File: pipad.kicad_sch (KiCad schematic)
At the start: 2 parts, among them J3 Conn_02x20_Odd_Even, J5 Conn_01x03

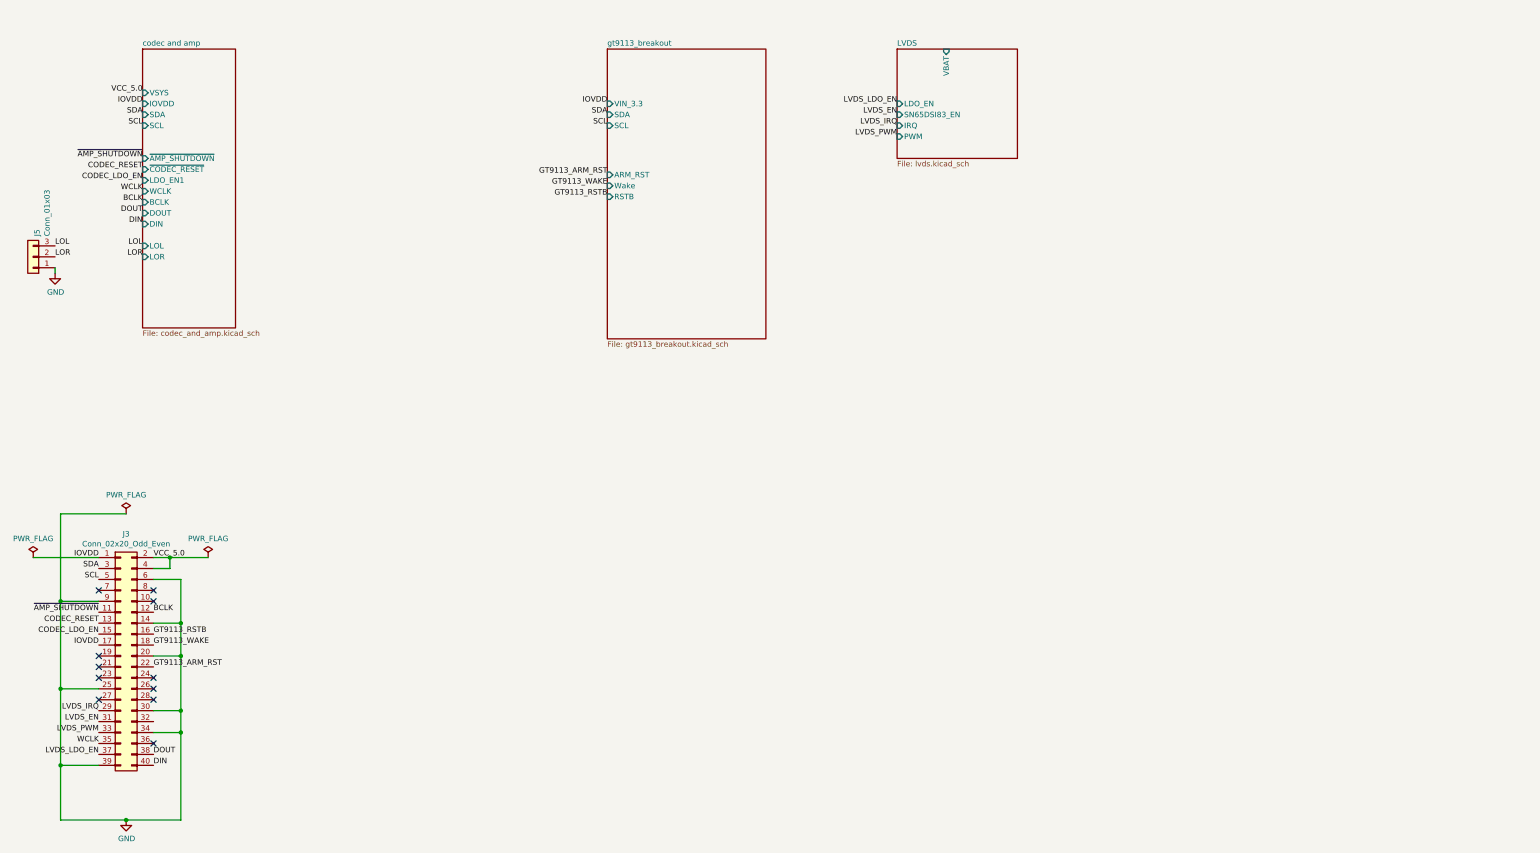
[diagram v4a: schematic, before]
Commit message: Add dock connector, battery pads, and ambient light sensor/compass connector. Switch Pi GPIO header from from THT to SMT so it is easier to place/route. Route differential signals for LVDS converter.
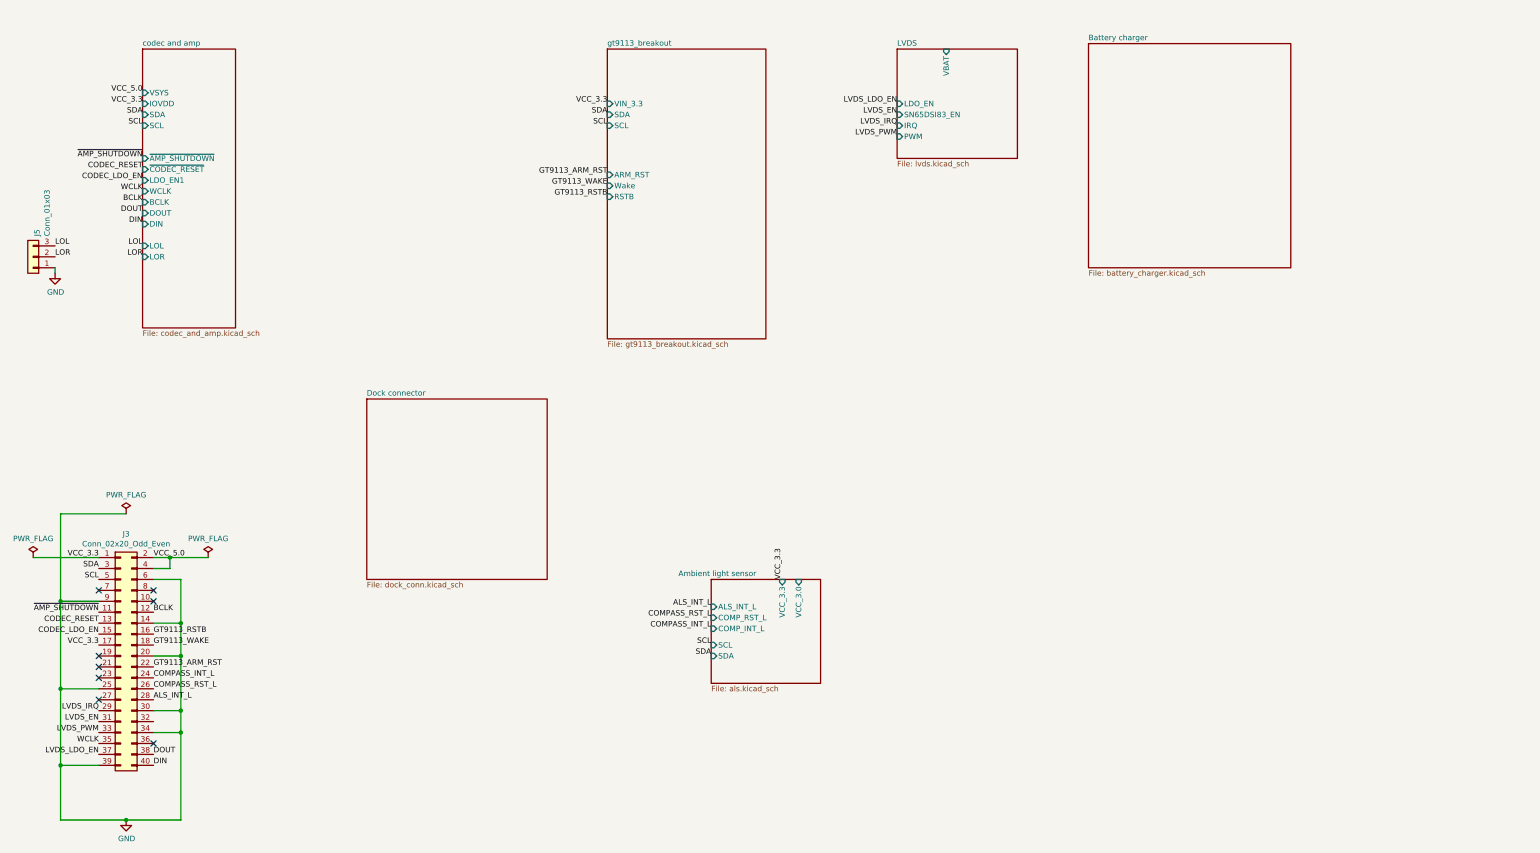
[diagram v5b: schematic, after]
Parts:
- J3: footprint Connector_PinHeader_2.54mm:PinHeader_2x20_P2.54mm_Vertical -> Connector_PinSocket_2.54mm:PinSocket_2x20_P2.54mm_Vertical_SMD
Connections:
- net COMPASS_INT_L: now reaches J3.24 (Pin_24)
- net COMPASS_RST_L: now reaches J3.26 (Pin_26)
- net ALS_INT_L: now reaches J3.28 (Pin_28)
- net IOVDD renamed VCC_3.3
- no-connect marks 11 -> 8
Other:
- added sheet Ambient light sensor (als.kicad_sch)
- added sheet Battery charger (battery_charger.kicad_sch)
- added sheet Dock connector (dock_conn.kicad_sch)
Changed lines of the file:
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@@
   (no_connect (at 62.23 163.83))
   (no_connect (at 62.23 166.37))
-  (no_connect (at 62.23 184.15))
-  (no_connect (at 62.23 186.69))
-  (no_connect (at 62.23 189.23))
   (no_connect (at 62.23 199.39))
   (wire (pts (xy 34.29 156.21) (xy 49.53 156.21))
@@
     (effects (font (size 1.27 1.27)) (justify left bottom))
   )
-  (label "IOVDD" (at 49.53 156.21 180)
+  (label "VCC_3.3" (at 49.53 156.21 180)
     (effects (font (size 1.27 1.27)) (justify right bottom))
   )
@@
     (effects (font (size 1.27 1.27)) (justify right bottom))
   )
-  (label "IOVDD" (at 49.53 176.53 180)
+  (label "VCC_3.3" (at 49.53 176.53 180)
     (effects (font (size 1.27 1.27)) (justify right bottom))
   )
@@
     (effects (font (size 1.27 1.27)) (justify right bottom))
   )
-  (label "IOVDD" (at 59.69 50.8 180)
+  (label "VCC_3.3" (at 59.69 50.8 180)
     (effects (font (size 1.27 1.27)) (justify right bottom))
   )
@@
     (effects (font (size 1.27 1.27)) (justify left bottom))
   )
+  (label "COMPASS_INT_L" (at 62.23 184.15 0)
+    (effects (font (size 1.27 1.27)) (justify left bottom))
+  )
+  (label "COMPASS_RST_L" (at 62.23 186.69 0)
+    (effects (font (size 1.27 1.27)) (justify left bottom))
+  )
+  (label "ALS_INT_L" (at 62.23 189.23 0)
+    (effects (font (size 1.27 1.27)) (justify left bottom))
+  )
   (label "DOUT" (at 62.23 201.93 0)
     (effects (font (size 1.27 1.27)) (justify left bottom))
@@
     (effects (font (size 1.27 1.27)) (justify left bottom))
   )
-  (label "IOVDD" (at 167.64 50.8 180)
+  (label "VCC_3.3" (at 167.64 50.8 180)
     (effects (font (size 1.27 1.27)) (justify right bottom))
   )
@@
   (label "GT9113_RSTB" (at 167.64 72.39 180)
     (effects (font (size 1.27 1.27)) (justify right bottom))
+  )
+  (label "ALS_INT_L" (at 191.77 167.64 180)
+    (effects (font (size 1.27 1.27)) (justify right bottom))
+  )
+  (label "COMPASS_RST_L" (at 191.77 170.18 180)
+    (effects (font (size 1.27 1.27)) (justify right bottom))
+  )
+  (label "COMPASS_INT_L" (at 191.77 172.72 180)
+    (effects (font (size 1.27 1.27)) (justify right bottom))
+  )
+  (label "SCL" (at 191.77 176.53 180)
+    (effects (font (size 1.27 1.27)) (justify right bottom))
+  )
+  (label "SDA" (at 191.77 179.07 180)
+    (effects (font (size 1.27 1.27)) (justify right bottom))
+  )
+  (label "VCC_3.3" (at 208.28 161.29 90)
+    (effects (font (size 1.27 1.27)) (justify left bottom))
   )
   (label "LVDS_LDO_EN" (at 234.95 50.8 180)
@@
     (property "Reference" "J3" (id 0) (at 55.88 150.7298 0))
     (property "Value" "Conn_02x20_Odd_Even" (id 1) (at 55.88 153.0285 0))
-    (property "Footprint" "Connector_PinHeader_2.54mm:PinHeader_2x20_P2.54mm_Vertical" (id 2) (at 54.61 179.07 0)
+    (property "Footprint" "Connector_PinSocket_2.54mm:PinSocket_2x20_P2.54mm_Vertical_SMD" (id 2) (at 54.61 179.07 0)
       (effects (font (size 1.27 1.27)) hide)
     )
@@
     (pin "9")
   )
+  (sheet (at 191.77 161.29) (size 25.4 24.13)
+    (stroke (width 0.0006) (type solid) (color 0 0 0 0))
+    (fill (color 0 0 0 0.0000))
+    (property "Sheet name" "Ambient light sensor" (id 0) (at 184.15 160.6543 0)
+      (effects (font (size 1.27 1.27)) (justify left bottom))
+    )
+    (property "Sheet file" "als.kicad_sch" (id 1) (at 191.77 185.9287 0)
+      (effects (font (size 1.27 1.27)) (justify left top))
+    )
+    (pin "ALS_INT_L" input (at 191.77 167.64 180)
+      (effects (font (size 1.27 1.27)) (justify left))
+    )
+    (pin "VCC_3.0" input (at 212.09 161.29 90)
+      (effects (font (size 1.27 1.27)) (justify right))
+    )
+    (pin "COMP_RST_L" input (at 191.77 170.18 180)
+      (effects (font (size 1.27 1.27)) (justify left))
+    )
+    (pin "COMP_INT_L" input (at 191.77 172.72 180)
+      (effects (font (size 1.27 1.27)) (justify left))
+    )
+    (pin "VCC_3.3" input (at 208.28 161.29 90)
+      (effects (font (size 1.27 1.27)) (justify right))
+    )
+    (pin "SCL" input (at 191.77 176.53 180)
+      (effects (font (size 1.27 1.27)) (justify left))
+    )
+    (pin "SDA" input (at 191.77 179.07 180)
+      (effects (font (size 1.27 1.27)) (justify left))
+    )
+  )
+  (sheet (at 279.4 36.83) (size 46.99 52.07) (fields_autoplaced)
+    (stroke (width 0.0006) (type solid) (color 0 0 0 0))
+    (fill (color 0 0 0 0.0000))
+    (property "Sheet name" "Battery charger" (id 0) (at 279.4 36.1943 0)
+      (effects (font (size 1.27 1.27)) (justify left bottom))
+    )
+    (property "Sheet file" "battery_charger.kicad_sch" (id 1) (at 279.4 89.4087 0)
+      (effects (font (size 1.27 1.27)) (justify left top))
+    )
+  )
+  (sheet (at 111.76 119.38) (size 41.91 41.91) (fields_autoplaced)
+    (stroke (width 0.0006) (type solid) (color 0 0 0 0))
+    (fill (color 0 0 0 0.0000))
+    (property "Sheet name" "Dock connector" (id 0) (at 111.76 118.7443 0)
+      (effects (font (size 1.27 1.27)) (justify left bottom))
+    )
+    (property "Sheet file" "dock_conn.kicad_sch" (id 1) (at 111.76 161.7987 0)
+      (effects (font (size 1.27 1.27)) (justify left top))
+    )
+  )
   (sheet (at 234.95 38.1) (size 27.94 25.4) (fields_autoplaced)
     (stroke (width 0.0006) (type solid) (color 0 0 0 0))
@@
     (path "/4ecc04d7-c0c4-4778-83ba-d295a895ebe9/" (page "5"))
     (path "/1cd8b29a-6edd-403b-84dd-3cf97c71d81a/" (page "6"))
+    (path "/eed4aa3c-bec9-4438-9bbd-324cd17b6734/" (page "7"))
+    (path "/593f2d4b-248b-4b7c-ad0b-1e77412a278c/" (page "8"))
+    (path "/edc6f2df-f35f-4519-8662-3f6b046c5ebe/" (page "9"))
     (path "/00000000-0000-0000-0000-00006026a3be/e9fc4bb6-5bde-4905-9630-250663643427/" (page " "))
   )
@@
     )
     (path "/c8db29bf-2e44-49e3-93a1-10d1ae7e3bc6"
-      (reference "J3") (unit 1) (value "Conn_02x20_Odd_Even") (footprint "Connector_PinHeader_2.54mm:PinHeader_2x20_P2.54mm_Vertical")
+      (reference "J3") (unit 1) (value "Conn_02x20_Odd_Even") (footprint "Connector_PinSocket_2.54mm:PinSocket_2x20_P2.54mm_Vertical_SMD")
     )
     (path "/00000000-0000-0000-0000-00006042168e"
@@
     )
     (path "/00000000-0000-0000-0000-00006026a3be/b55ef69f-163d-4993-9382-858066625f10"
-      (reference "C24") (unit 1) (value "10uF") (footprint "Capacitor_SMD:C_0402_1005Metric")
+      (reference "C24") (unit 1) (value "100nF") (footprint "Capacitor_SMD:C_0402_1005Metric")
     )
     (path "/00000000-0000-0000-0000-00006026a3be/00000000-0000-0000-0000-000060262be3"
@@
       (reference "U13") (unit 1) (value "MIC5504-1.8YM5") (footprint "Package_TO_SOT_SMD:SOT-23-5")
     )
+    (path "/eed4aa3c-bec9-4438-9bbd-324cd17b6734/b7269330-1a8b-4d32-8cbf-f9de4c1809fa"
+      (reference "#PWR0124") (unit 1) (value "GND") (footprint "")
+    )
+    (path "/eed4aa3c-bec9-4438-9bbd-324cd17b6734/80125fd9-cbee-474e-bd31-4c8328a3ee11"
+      (reference "J8") (unit 1) (value "Conn_01x04") (footprint "footprints:ipad battery connector")
+    )
+    (path "/593f2d4b-248b-4b7c-ad0b-1e77412a278c/b6c17278-80cb-4a53-bf13-61b8e469c5ec"
+      (reference "J10") (unit 1) (value "Conn_02x35_Odd_Even") (footprint "footprints:Panasonic-AXK770147G-MFG")
+    )
+    (path "/edc6f2df-f35f-4519-8662-3f6b046c5ebe/4a52f7a8-b3bb-49ea-bf5d-c5cfb91d46fd"
+      (reference "#PWR0125") (unit 1) (value "GND") (footprint "")
+    )
+    (path "/edc6f2df-f35f-4519-8662-3f6b046c5ebe/6b9ea1a1-01bb-4fbc-bc7e-d4b5612b58b0"
+      (reference "#PWR0126") (unit 1) (value "GND") (footprint "")
+    )
+    (path "/edc6f2df-f35f-4519-8662-3f6b046c5ebe/78022ed6-df53-4a6b-a7fd-76294b2fec4e"
+      (reference "J11") (unit 1) (value "Conn_02x12_Odd_Even") (footprint "footprints:AA03-S024VA1")
+    )
+    (path "/edc6f2df-f35f-4519-8662-3f6b046c5ebe/93f53bed-e069-4f03-aa65-267475a61a1d"
+      (reference "U14") (unit 1) (value "TCA9802") (footprint "Package_SO:VSSOP-8_3.0x3.0mm_P0.65mm")
+    )
     (path "/00000000-0000-0000-0000-00006026a3be/e9fc4bb6-5bde-4905-9630-250663643427/fd649b90-fe8e-4ecf-a531-c62c874ce18c"

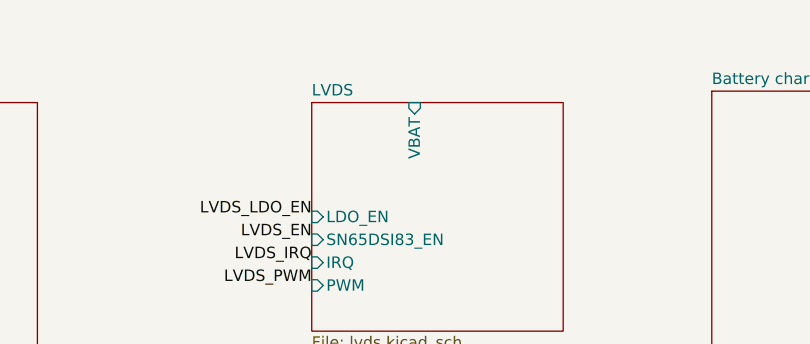
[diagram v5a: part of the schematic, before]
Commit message: Change DSI connector to the 15-pin standard instead of 22-pin standard
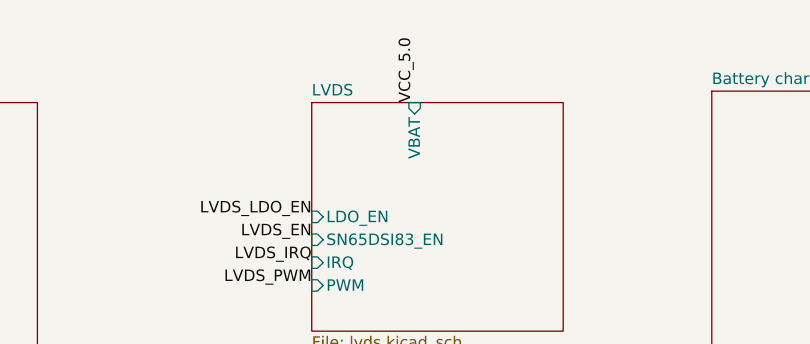
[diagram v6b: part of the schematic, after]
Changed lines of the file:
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@@
     (effects (font (size 1.27 1.27)) (justify right bottom))
+  )
+  (label "VCC_5.0" (at 246.38 38.1 90)
+    (effects (font (size 1.27 1.27)) (justify left bottom))
   )
   (symbol (lib_id "power:PWR_FLAG") (at 34.29 156.21 0) (unit 1)
@@
       (reference "#PWR018") (unit 1) (value "GND") (footprint "")
     )
+    (path "/1cd8b29a-6edd-403b-84dd-3cf97c71d81a/789b6274-204a-4135-a0e4-58a250d98bc4"
+      (reference "#PWR019") (unit 1) (value "GND") (footprint "")
+    )
     (path "/1cd8b29a-6edd-403b-84dd-3cf97c71d81a/a845cb81-e330-48d6-8331-ea5663b2a5b2"
       (reference "#PWR022") (unit 1) (value "GND") (footprint "")
@@
       (reference "#PWR034") (unit 1) (value "GND") (footprint "")
     )
+    (path "/1cd8b29a-6edd-403b-84dd-3cf97c71d81a/0661f722-766f-44a6-9d35-fcf651df4232"
+      (reference "#PWR035") (unit 1) (value "GND") (footprint "")
+    )
     (path "/1cd8b29a-6edd-403b-84dd-3cf97c71d81a/4176f006-1e85-4f72-886c-602afcf82e4f"
       (reference "#PWR0121") (unit 1) (value "GND") (footprint "")
     )
+    (path "/1cd8b29a-6edd-403b-84dd-3cf97c71d81a/c941db41-80d0-4c59-ac00-a75f75bce51b"
+      (reference "#PWR0127") (unit 1) (value "GND") (footprint "")
+    )
+    (path "/1cd8b29a-6edd-403b-84dd-3cf97c71d81a/83a0926b-3f0c-476b-b123-9bf9bf3de2c4"
+      (reference "#PWR0128") (unit 1) (value "GND") (footprint "")
+    )
     (path "/1cd8b29a-6edd-403b-84dd-3cf97c71d81a/1236932b-e848-47c3-a615-22b04b990ea2"
-      (reference "C28") (unit 1) (value "10uF") (footprint "Capacitor_SMD:C_0402_1005Metric_Pad0.74x0.62mm_HandSolder")
+      (reference "C28") (unit 1) (value "10uF") (footprint "Capacitor_SMD:C_0402_1005Metric")
     )
     (path "/1cd8b29a-6edd-403b-84dd-3cf97c71d81a/1ac7e510-1100-4a2f-917e-efeeba2df0f2"
-      (reference "C29") (unit 1) (value "100nF") (footprint "Capacitor_SMD:C_0402_1005Metric_Pad0.74x0.62mm_HandSolder")
+      (reference "C29") (unit 1) (value "100nF") (footprint "Capacitor_SMD:C_0402_1005Metric")
     )
     (path "/1cd8b29a-6edd-403b-84dd-3cf97c71d81a/9d794519-61b7-40e3-aa97-9bcb139f12aa"
-      (reference "C30") (unit 1) (value "100nF") (footprint "Capacitor_SMD:C_0402_1005Metric_Pad0.74x0.62mm_HandSolder")
+      (reference "C30") (unit 1) (value "100nF") (footprint "Capacitor_SMD:C_0402_1005Metric")
     )
     (path "/1cd8b29a-6edd-403b-84dd-3cf97c71d81a/66d10ad5-68bd-401f-9224-86cfa06dbb17"
-      (reference "C31") (unit 1) (value "100nF") (footprint "Capacitor_SMD:C_0402_1005Metric_Pad0.74x0.62mm_HandSolder")
+      (reference "C31") (unit 1) (value "100nF") (footprint "Capacitor_SMD:C_0402_1005Metric")
     )
     (path "/1cd8b29a-6edd-403b-84dd-3cf97c71d81a/1b379949-29e3-4890-b390-f9a895be3273"
-      (reference "C32") (unit 1) (value "100nF") (footprint "Capacitor_SMD:C_0402_1005Metric_Pad0.74x0.62mm_HandSolder")
+      (reference "C32") (unit 1) (value "100nF") (footprint "Capacitor_SMD:C_0402_1005Metric")
     )
     (path "/1cd8b29a-6edd-403b-84dd-3cf97c71d81a/57252608-cf95-4018-939d-750f564af1a3"
-      (reference "C33") (unit 1) (value "100nF") (footprint "Capacitor_SMD:C_0402_1005Metric_Pad0.74x0.62mm_HandSolder")
+      (reference "C33") (unit 1) (value "100nF") (footprint "Capacitor_SMD:C_0402_1005Metric")
     )
     (path "/1cd8b29a-6edd-403b-84dd-3cf97c71d81a/d57f3955-4f73-47b5-a137-ca3e4ca1983b"
-      (reference "C34") (unit 1) (value "1uF") (footprint "Capacitor_SMD:C_0402_1005Metric_Pad0.74x0.62mm_HandSolder")
+      (reference "C34") (unit 1) (value "1uF") (footprint "Capacitor_SMD:C_0402_1005Metric")
     )
     (path "/1cd8b29a-6edd-403b-84dd-3cf97c71d81a/9cdda166-05ca-4281-8fc8-9d347bd2ef07"
-      (reference "C35") (unit 1) (value "100nF") (footprint "Capacitor_SMD:C_0402_1005Metric_Pad0.74x0.62mm_HandSolder")
+      (reference "C35") (unit 1) (value "100nF") (footprint "Capacitor_SMD:C_0402_1005Metric")
     )
     (path "/1cd8b29a-6edd-403b-84dd-3cf97c71d81a/9b45f2c8-f3f9-4963-a243-30be42198924"
-      (reference "C36") (unit 1) (value "100nF") (footprint "Capacitor_SMD:C_0402_1005Metric_Pad0.74x0.62mm_HandSolder")
+      (reference "C36") (unit 1) (value "100nF") (footprint "Capacitor_SMD:C_0402_1005Metric")
     )
     (path "/1cd8b29a-6edd-403b-84dd-3cf97c71d81a/39e91bac-6f61-474f-9d4e-1d78b4b44636"
-      (reference "C37") (unit 1) (value "100nF") (footprint "Capacitor_SMD:C_0402_1005Metric_Pad0.74x0.62mm_HandSolder")
+      (reference "C37") (unit 1) (value "100nF") (footprint "Capacitor_SMD:C_0402_1005Metric")
     )
     (path "/1cd8b29a-6edd-403b-84dd-3cf97c71d81a/324c2d85-ee3d-4531-a1fd-5025a4f3530f"
-      (reference "C38") (unit 1) (value "100nF") (footprint "Capacitor_SMD:C_0402_1005Metric_Pad0.74x0.62mm_HandSolder")
+      (reference "C38") (unit 1) (value "100nF") (footprint "Capacitor_SMD:C_0402_1005Metric")
     )
     (path "/1cd8b29a-6edd-403b-84dd-3cf97c71d81a/96cd089e-bf72-4ce9-8e8a-05dc35c3433e"
-      (reference "C39") (unit 1) (value "100nF") (footprint "Capacitor_SMD:C_0402_1005Metric_Pad0.74x0.62mm_HandSolder")
+      (reference "C39") (unit 1) (value "100nF") (footprint "Capacitor_SMD:C_0402_1005Metric")
     )
     (path "/1cd8b29a-6edd-403b-84dd-3cf97c71d81a/3cf2c34e-3928-4b71-b049-02f477bcf0ec"
-      (reference "C40") (unit 1) (value "100nF") (footprint "Capacitor_SMD:C_0402_1005Metric_Pad0.74x0.62mm_HandSolder")
+      (reference "C40") (unit 1) (value "100nF") (footprint "Capacitor_SMD:C_0402_1005Metric")
     )
     (path "/1cd8b29a-6edd-403b-84dd-3cf97c71d81a/2ca0862f-8491-467b-a5fa-ce6cf170020f"
-      (reference "C41") (unit 1) (value "100nF") (footprint "Capacitor_SMD:C_0402_1005Metric_Pad0.74x0.62mm_HandSolder")
+      (reference "C41") (unit 1) (value "100nF") (footprint "Capacitor_SMD:C_0402_1005Metric")
     )
     (path "/1cd8b29a-6edd-403b-84dd-3cf97c71d81a/883bde91-7d01-40cd-8bac-556ba2d2b550"
-      (reference "C42") (unit 1) (value "1uF") (footprint "Capacitor_SMD:C_0402_1005Metric_Pad0.74x0.62mm_HandSolder")
+      (reference "C42") (unit 1) (value "1uF") (footprint "Capacitor_SMD:C_0402_1005Metric")
     )
     (path "/1cd8b29a-6edd-403b-84dd-3cf97c71d81a/a44a58be-109e-4f11-bb12-5b305446830c"
-      (reference "C43") (unit 1) (value "0.47uF") (footprint "Capacitor_SMD:C_0402_1005Metric_Pad0.74x0.62mm_HandSolder")
+      (reference "C43") (unit 1) (value "0.47uF") (footprint "Capacitor_SMD:C_0402_1005Metric")
     )
     (path "/1cd8b29a-6edd-403b-84dd-3cf97c71d81a/2e0ec137-0224-4b2a-b8ec-01b49fa4194d"
-      (reference "C44") (unit 1) (value "4.7uF") (footprint "Capacitor_SMD:C_0402_1005Metric_Pad0.74x0.62mm_HandSolder")
+      (reference "C44") (unit 1) (value "4.7uF") (footprint "Capacitor_SMD:C_0402_1005Metric")
+    )
+    (path "/1cd8b29a-6edd-403b-84dd-3cf97c71d81a/369438df-81da-4173-90c2-ed7ac4bdbaa5"
+      (reference "C45") (unit 1) (value "10uF") (footprint "Capacitor_SMD:C_0402_1005Metric")
+    )
+    (path "/1cd8b29a-6edd-403b-84dd-3cf97c71d81a/0c2e18c5-09de-43ee-8f72-c0182e49c223"
+      (reference "C46") (unit 1) (value "2.2uF") (footprint "Capacitor_SMD:C_0402_1005Metric")
     )
     (path "/1cd8b29a-6edd-403b-84dd-3cf97c71d81a/2e2bd6a2-0649-4331-8eef-bb523aed6947"
@@
     )
     (path "/1cd8b29a-6edd-403b-84dd-3cf97c71d81a/546be596-3aa6-4c3f-acd9-b48839fb0e99"
-      (reference "J4") (unit 1) (value "Conn_01x22_Female") (footprint "Connector_FFC-FPC:Hirose_FH12-22S-0.5SH_1x22-1MP_P0.50mm_Horizontal")
+      (reference "J4") (unit 1) (value "Conn_01x15_Female") (footprint "footprints:SFW15R-2STE1LF")
     )
     (path "/1cd8b29a-6edd-403b-84dd-3cf97c71d81a/a765b945-47c1-486b-90c7-1176b9aaf6b5"
